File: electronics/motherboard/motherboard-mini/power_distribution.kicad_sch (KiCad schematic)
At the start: 58 parts, among them J6 2604-3102, J7 SOLAR_CRNT_JMPR, J8 BAT_CRNT_JMPR, J9 2604-3102, U3 INA219BxD, U4 LT3652IMSE, U5 MCP73832-2-OT, U6 INA219BxD, U7 MIC2288YD5-TR, U8 XC6215B332MR-G, U9 NCP718xSN500

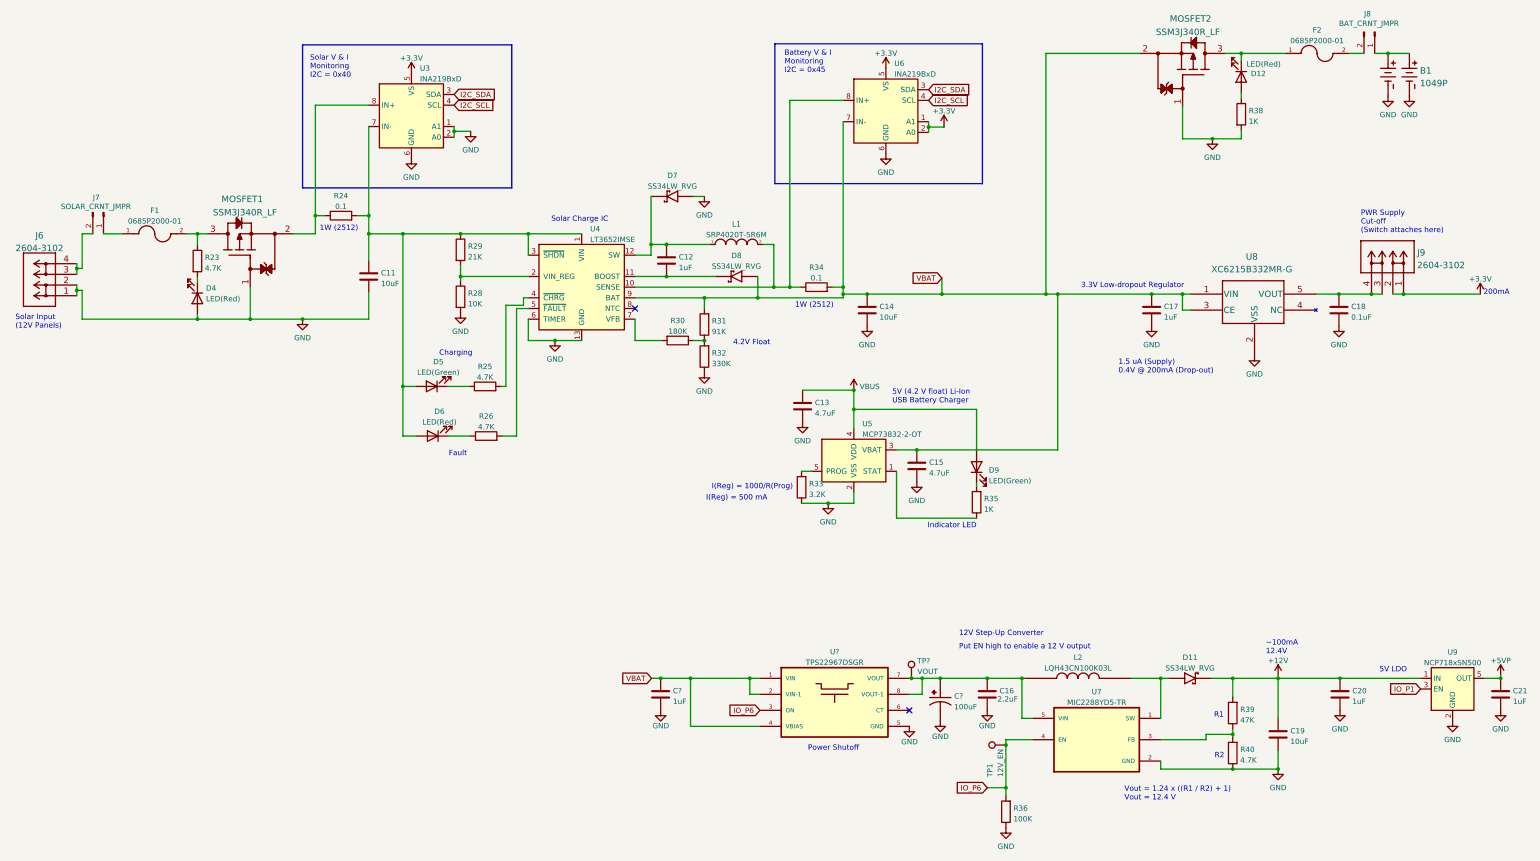
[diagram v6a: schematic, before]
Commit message: new version sent for manufacture, updated component positioning, removed level shifter on SDI-12 line, re routed the solar charge circuit
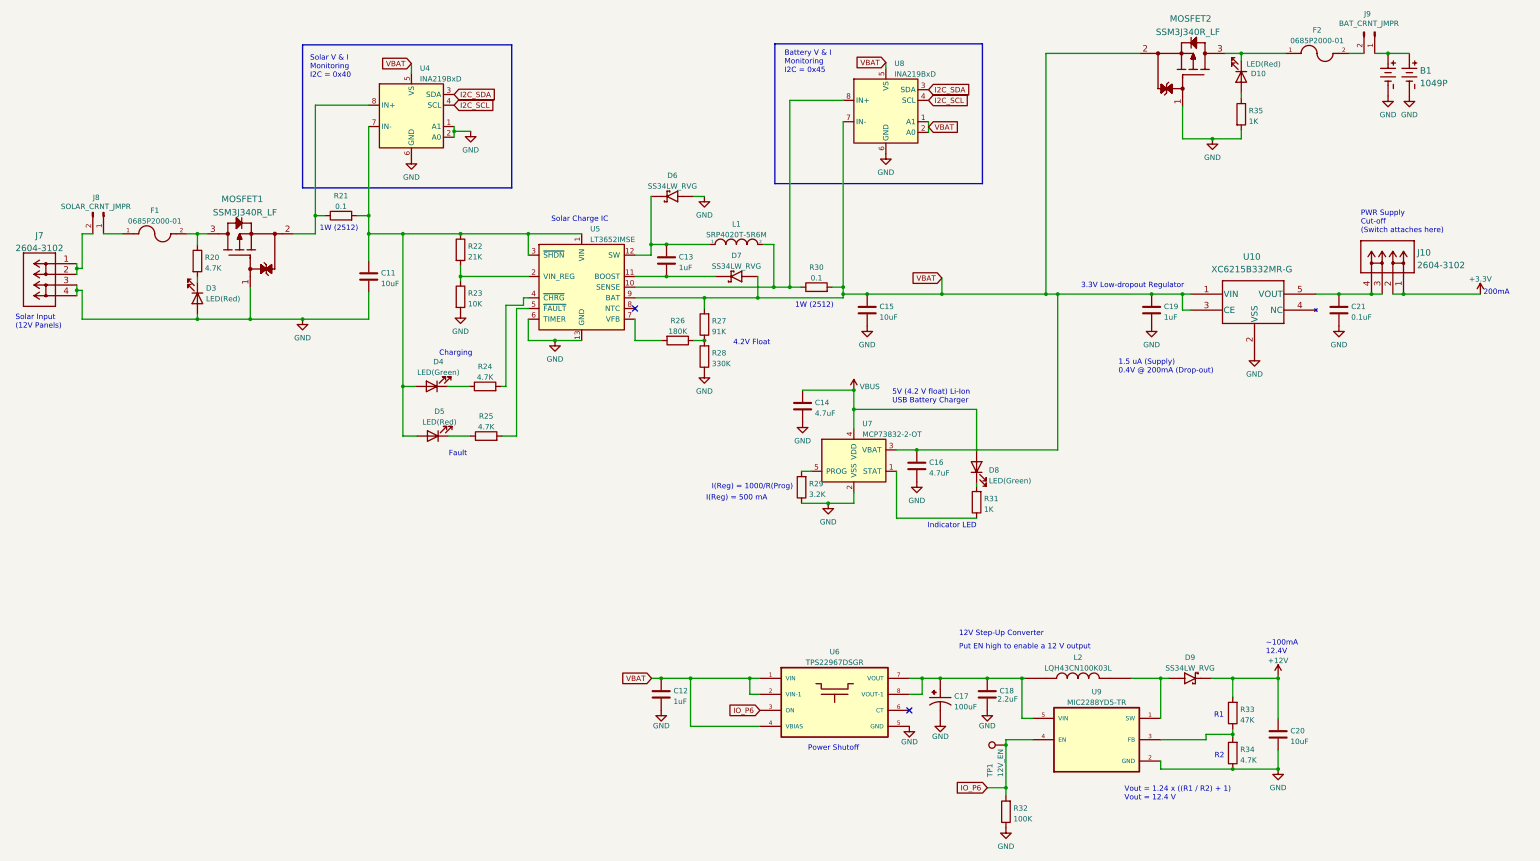
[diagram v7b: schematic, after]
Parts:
- removed C20, C21: 1uF, Capacitor_SMD:C_0805_2012Metric, symbol Device:C
- removed TP?: VOUT, TestPoint:TestPoint_Pad_D1.0mm, symbol Connector:TestPoint
- removed U9: NCP718xSN500, Package_TO_SOT_SMD:SOT-23-5, symbol Regulator_Linear:NCP718xSN500
- gave numbers to parts that had none: 3
- renumbered C12 to C13, C13 to C14, C14 to C15, C15 to C16, C16 to C18, C17 to C19, C19 to C20, C18 to C21, D12 to D10, D4 to D3, D5 to D4, D6 to D5, D7 to D6, D8 to D7, D9 to D8, D11 to D9, J9 to J10, J6 to J7, J7 to J8, J8 to J9, R23 to R20, R24 to R21, R29 to R22, R28 to R23, R25 to R24, R26 to R25, R30 to R26, R31 to R27, R32 to R28, R33 to R29, R34 to R30, R35 to R31, R36 to R32, R39 to R33, R40 to R34, R38 to R35, U8 to U10, U3 to U4, U4 to U5, U5 to U7, U6 to U8, U7 to U9
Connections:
- net +3.3V: no longer U4.5 (VS), U8.1 (A1), U8.2 (A0), U8.5 (VS)
- net GND: now also J7.3, J7.4; no longer J7.1, J7.2
- net VBAT: now also U4.5 (VS), U8.1 (A1), U8.2 (A0), U8.5 (VS)
- new net: J7.1, J7.2, J8.2 (Pin_2)
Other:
- note removed: "5V LDO"
- moved on the sheet: J7

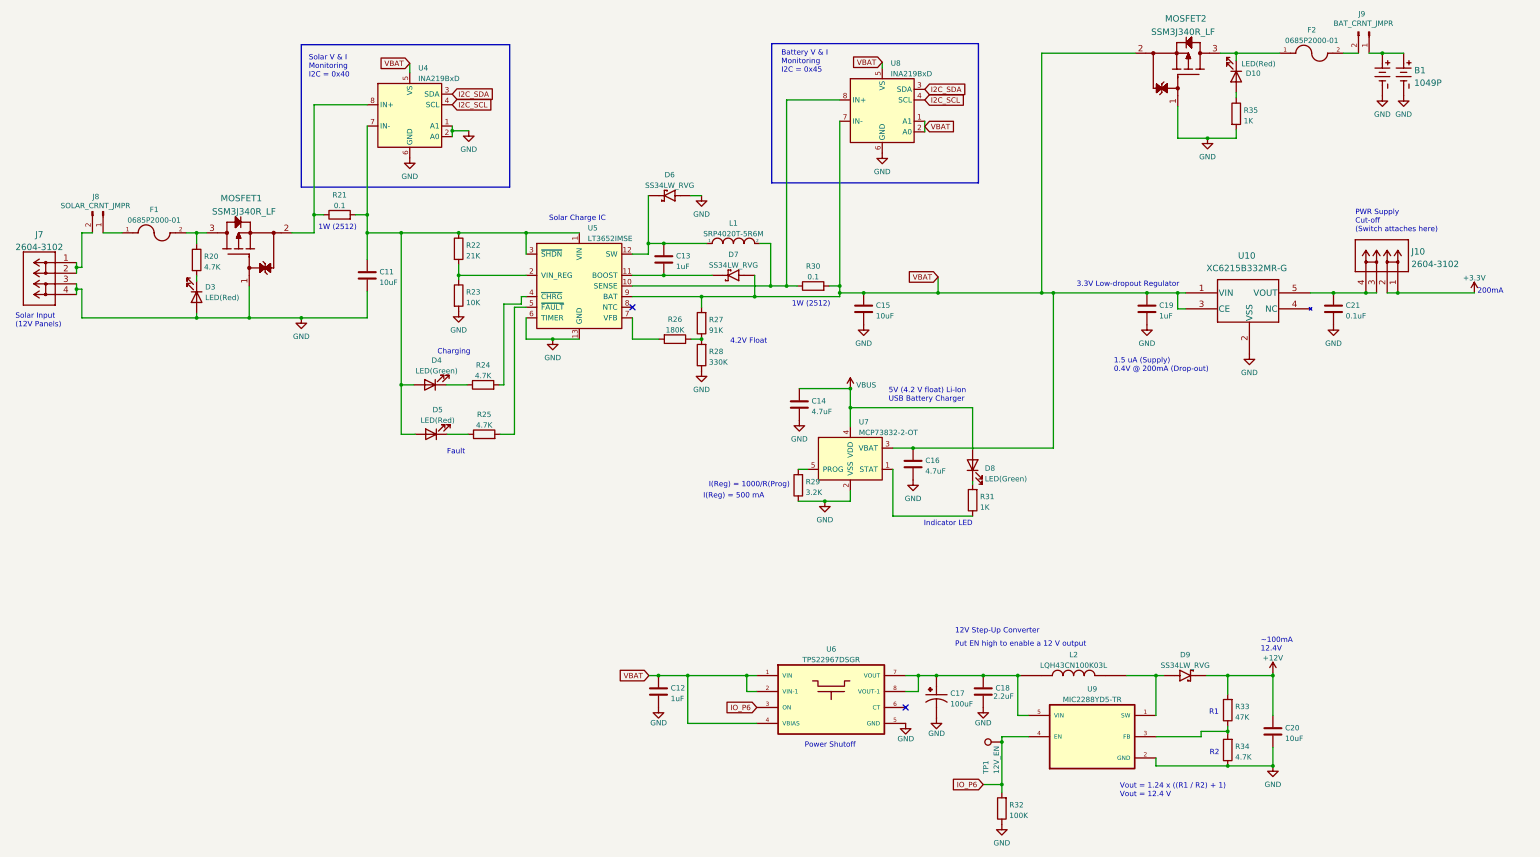
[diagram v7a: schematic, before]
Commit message: refactored schemematics and added pdf previews for readme
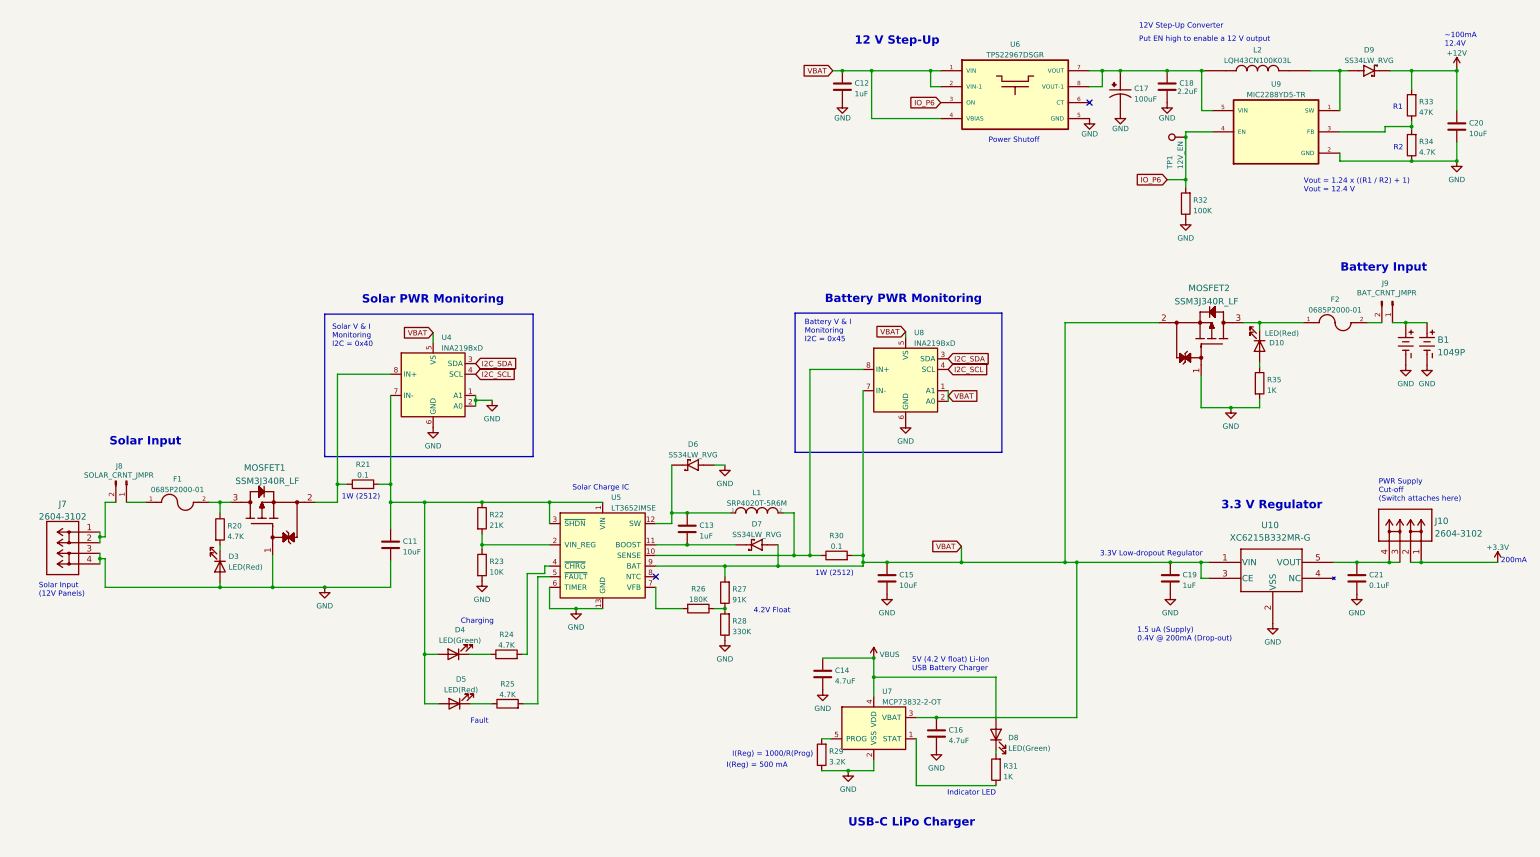
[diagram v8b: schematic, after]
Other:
- note added: "12 V Step-Up"
- note added: "3.3 V Regulator"
- note added: "Battery Input"
- note added: "Battery PWR Monitoring"
- note added: "Solar Input"
- note added: "Solar PWR Monitoring"
- note added: "USB-C LiPo Charger"
- company: (none) -> NSW Department of Primary Industries
- title: (none) -> Enviro-node
- moved on the sheet: B1, C11, C12, C13, C14, C15, C16, C17, C18, C19, C20, C21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
